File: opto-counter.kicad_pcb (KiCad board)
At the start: 2 copper layers, 27.9 x 27.9 mm, 13 parts, among them J1 IR-REC, J2 qwiic, J3 UPDI, U1 ATtiny404-SS, U2 TSSP6038

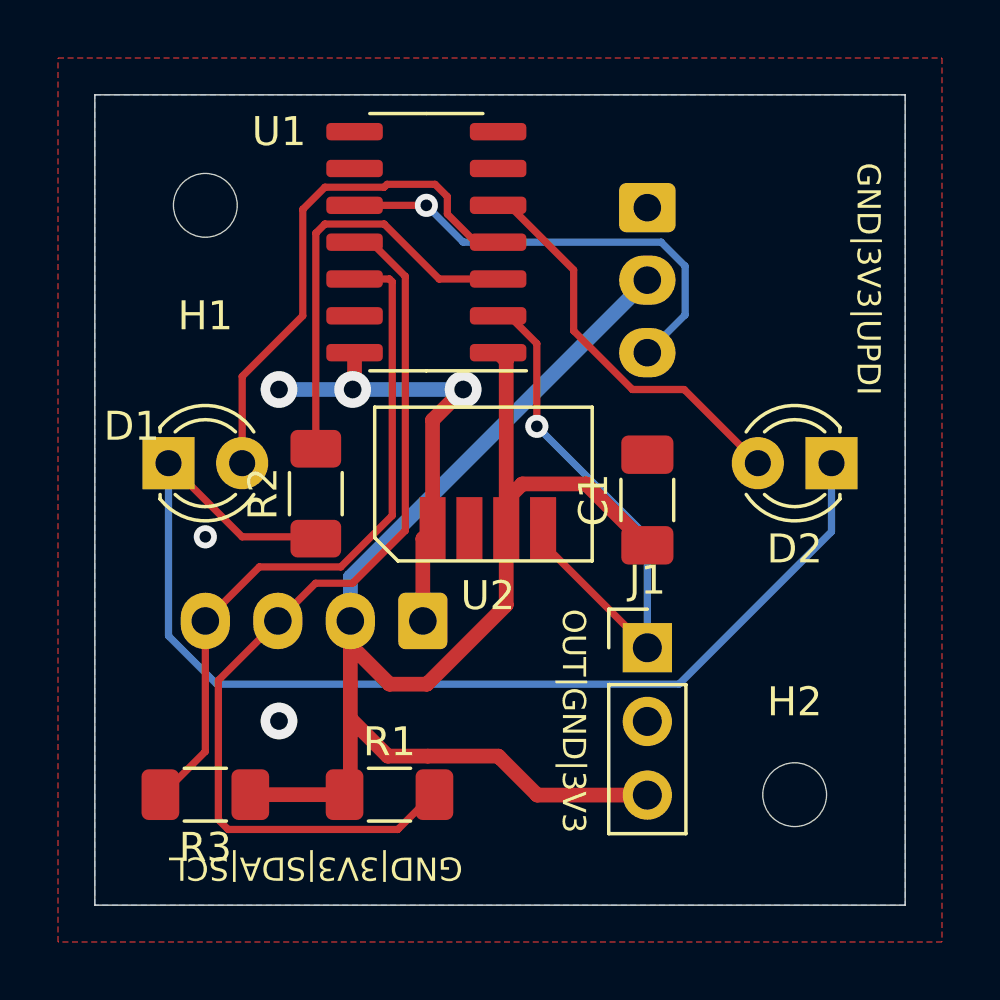
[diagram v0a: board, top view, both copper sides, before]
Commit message: Remove temporary library `opto-counter-rescue`
Also add forgotten `fp-lib-table` and small changes to the PCB.
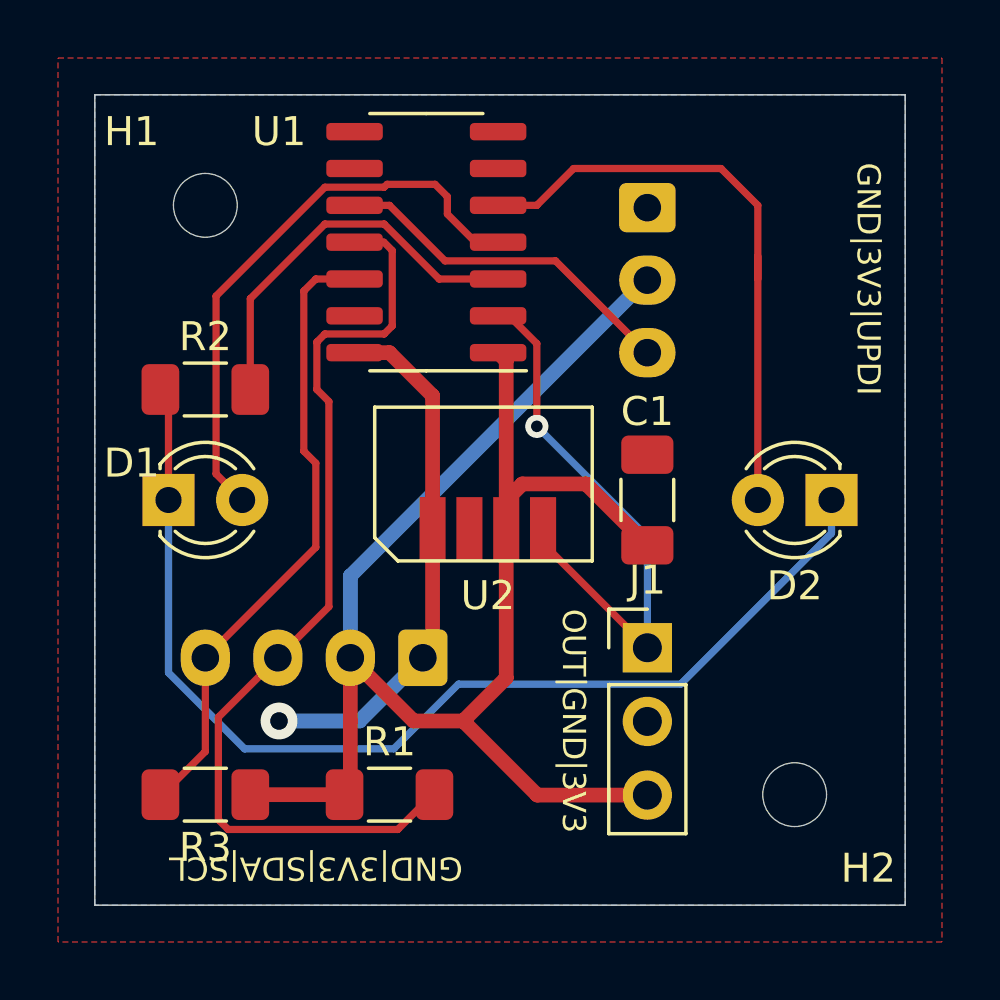
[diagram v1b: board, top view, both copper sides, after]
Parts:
- moved R2 5.24 mm to (67.3, 34.3), turned to 0 degrees
- moved D1 1.27 mm to (66.0, 38.1)
- moved D2 1.27 mm to (88.9, 38.1)
- moved J2 1.27 mm to (74.8, 43.5)
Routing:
- net Net-(D2-A): track 13.9 -> 21.0 mm
- net UPDI: track 15.8 -> 12.2 mm, vias 1 -> 0
- net +3V3: track 59.5 -> 56.4 mm
- net SCL: track 24.0 -> 21.7 mm
- net GND: track 16.2 -> 18.3 mm, vias 5 -> 1
- net Net-(D1-K): track 40.2 -> 38.1 mm
- net Net-(D1-A): track 17.9 -> 19.9 mm
- net Net-(U1-PA5): track 14.7 -> 13.5 mm
- net SDA: track 32.4 -> 33.1 mm

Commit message: Small improvements and fixes in the PCB, generated new gerbers files
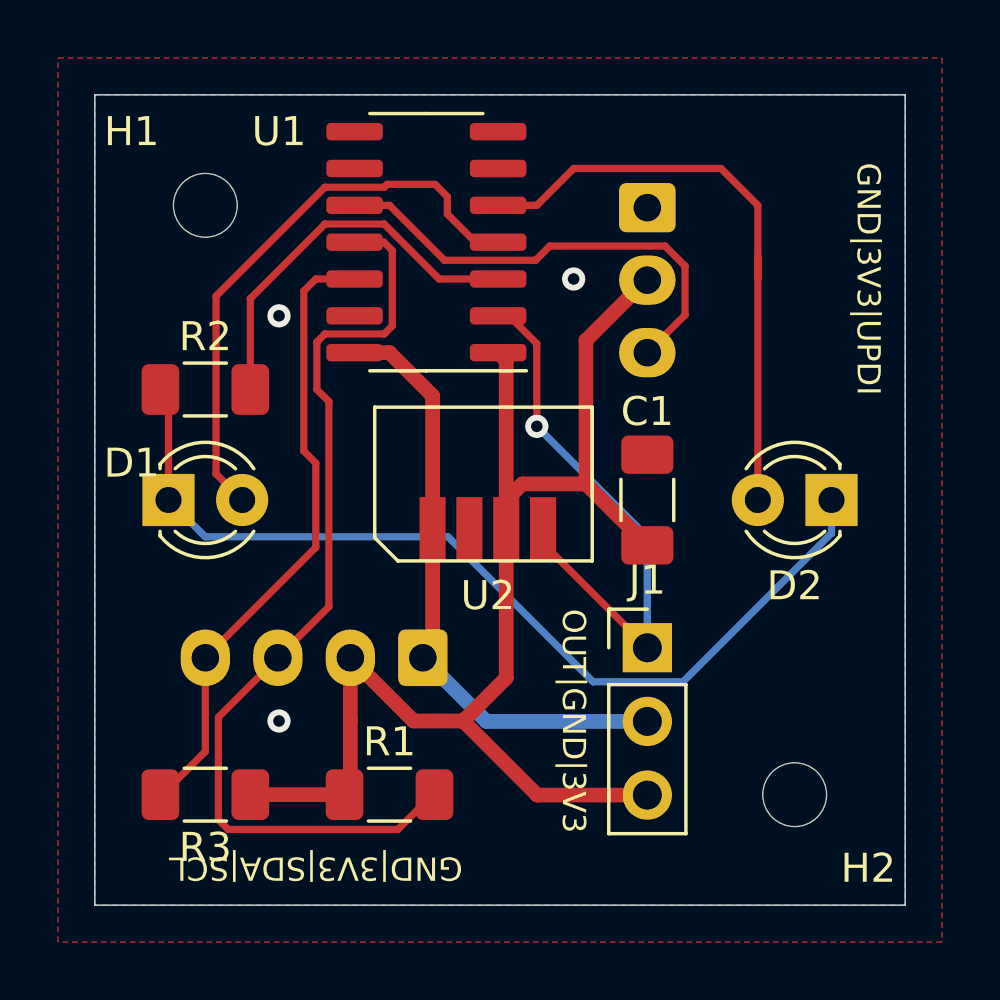
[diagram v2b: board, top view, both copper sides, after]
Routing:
- net +3V3: track 56.4 -> 47.0 mm
- net Net-(D1-K): track 38.1 -> 32.7 mm
- net UPDI: track 12.2 -> 16.2 mm
- net GND: track 18.3 -> 21.1 mm, vias 1 -> 3
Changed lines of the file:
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@@
       (plot_on_all_layers_selection 0x0000000_00000000)
       (disableapertmacros false)
-      (usegerberextensions false)
+      (usegerberextensions true)
       (usegerberattributes true)
       (usegerberadvancedattributes true)
-      (creategerberjobfile true)
+      (creategerberjobfile false)
       (dashed_line_dash_ratio 12.000000)
       (dashed_line_gap_ratio 3.000000)
@@
       (plotinvisibletext false)
       (sketchpadsonfab false)
-      (subtractmaskfromsilk false)
+      (subtractmaskfromsilk true)
       (outputformat 1)
       (mirror false)
@@
     (fp_line (start 1.6 0.8) (end -1.6 0.8)
       (stroke (width 0.1) (type solid)) (layer "F.Fab"))
-    (pad "1" smd roundrect (at -1.5625 0 90) (size 1.325 1.8) (layers "F.Cu" "F.Paste" "F.Mask") (roundrect_rratio 0.188679)
+    (pad "1" smd roundrect (at -1.5625 0 90) (size 1.325 1.8) (layers "F.Cu" "F.Paste" "F.Mask") (roundrect_rratio 0.1886792453)
       (net 1 "+3V3") (pintype "passive"))
-    (pad "2" smd roundrect (at 1.5625 0 90) (size 1.325 1.8) (layers "F.Cu" "F.Paste" "F.Mask") (roundrect_rratio 0.188679)
+    (pad "2" smd roundrect (at 1.5625 0 90) (size 1.325 1.8) (layers "F.Cu" "F.Paste" "F.Mask") (roundrect_rratio 0.1886792453)
       (net 2 "GND") (pintype "passive"))
     (model "${KICAD6_3DMODEL_DIR}/Capacitor_SMD.3dshapes/C_1206_3216Metric.wrl"
@@
     (fp_line (start 1.6 0.8) (end -1.6 0.8)
       (stroke (width 0.1) (type solid)) (layer "F.Fab"))
-    (pad "1" smd roundrect (at -1.55 0) (size 1.3 1.75) (layers "F.Cu" "F.Paste" "F.Mask") (roundrect_rratio 0.192308)
+    (pad "1" smd roundrect (at -1.55 0) (size 1.3 1.75) (layers "F.Cu" "F.Paste" "F.Mask") (roundrect_rratio 0.1923076923)
       (net 1 "+3V3") (pintype "passive"))
-    (pad "2" smd roundrect (at 1.55 0) (size 1.3 1.75) (layers "F.Cu" "F.Paste" "F.Mask") (roundrect_rratio 0.192308)
+    (pad "2" smd roundrect (at 1.55 0) (size 1.3 1.75) (layers "F.Cu" "F.Paste" "F.Mask") (roundrect_rratio 0.1923076923)
       (net 6 "SDA") (pintype "passive"))
     (model "${KICAD6_3DMODEL_DIR}/Resistor_SMD.3dshapes/R_1206_3216Metric.wrl"
@@
     (fp_line (start 1.6 0.8) (end -1.6 0.8)
       (stroke (width 0.1) (type solid)) (layer "F.Fab"))
-    (pad "1" smd roundrect (at -1.55 0) (size 1.3 1.75) (layers "F.Cu" "F.Paste" "F.Mask") (roundrect_rratio 0.192308)
+    (pad "1" smd roundrect (at -1.55 0) (size 1.3 1.75) (layers "F.Cu" "F.Paste" "F.Mask") (roundrect_rratio 0.1923076923)
       (net 3 "Net-(D1-K)") (pintype "passive"))
-    (pad "2" smd roundrect (at 1.55 0) (size 1.3 1.75) (layers "F.Cu" "F.Paste" "F.Mask") (roundrect_rratio 0.192308)
+    (pad "2" smd roundrect (at 1.55 0) (size 1.3 1.75) (layers "F.Cu" "F.Paste" "F.Mask") (roundrect_rratio 0.1923076923)
       (net 9 "Net-(U1-PA5)") (pintype "passive"))
     (model "${KICAD6_3DMODEL_DIR}/Resistor_SMD.3dshapes/R_1206_3216Metric.wrl"
@@
     (fp_line (start 1.6 0.8) (end -1.6 0.8)
       (stroke (width 0.1) (type solid)) (layer "F.Fab"))
-    (pad "1" smd roundrect (at -1.55 0 180) (size 1.3 1.75) (layers "F.Cu" "F.Paste" "F.Mask") (roundrect_rratio 0.192308)
+    (pad "1" smd roundrect (at -1.55 0 180) (size 1.3 1.75) (layers "F.Cu" "F.Paste" "F.Mask") (roundrect_rratio 0.1923076923)
       (net 1 "+3V3") (pintype "passive"))
-    (pad "2" smd roundrect (at 1.55 0 180) (size 1.3 1.75) (layers "F.Cu" "F.Paste" "F.Mask") (roundrect_rratio 0.192308)
+    (pad "2" smd roundrect (at 1.55 0 180) (size 1.3 1.75) (layers "F.Cu" "F.Paste" "F.Mask") (roundrect_rratio 0.1923076923)
       (net 7 "SCL") (pintype "passive"))
     (model "${KICAD6_3DMODEL_DIR}/Resistor_SMD.3dshapes/R_1206_3216Metric.wrl"
@@
     (fp_line (start 9.95 2.3) (end 8.75 2.3)
       (stroke (width 0.1) (type solid)) (layer "B.Fab"))
-    (pad "1" thru_hole roundrect (at 0 0 180) (size 1.7 1.95) (drill 0.95) (layers "*.Cu" "*.Mask") (roundrect_rratio 0.147059)
+    (pad "1" thru_hole roundrect (at 0 0 180) (size 1.7 1.95) (drill 0.95) (layers "*.Cu" "*.Mask") (roundrect_rratio 0.1470588235)
       (net 2 "GND") (pinfunction "Pin_1") (pintype "passive"))
     (pad "2" thru_hole oval (at 2.5 0 180) (size 1.7 1.95) (drill 0.95) (layers "*.Cu" "*.Mask")
@@
     (fp_line (start 7.45 2.3) (end 6.25 2.3)
       (stroke (width 0.1) (type solid)) (layer "B.Fab"))
-    (pad "1" thru_hole roundrect (at 0 0 270) (size 1.7 1.95) (drill 0.95) (layers "*.Cu" "*.Mask") (roundrect_rratio 0.147059)
+    (pad "1" thru_hole roundrect (at 0 0 270) (size 1.7 1.95) (drill 0.95) (layers "*.Cu" "*.Mask") (roundrect_rratio 0.1470588235)
       (net 2 "GND") (pinfunction "Pin_1") (pintype "passive"))
     (pad "2" thru_hole oval (at 2.5 0 270) (size 1.7 1.95) (drill 0.95) (layers "*.Cu" "*.Mask")
@@
   (segment (start 72.31 48.1225) (end 72.31 45.72) (width 0.508) (layer "F.Cu") (net 1))
   (segment (start 72.1725 48.26) (end 72.31 48.1225) (width 0.508) (layer "F.Cu") (net 1))
+  (segment (start 82.55 30.48) (end 80.4335 32.5965) (width 0.508) (layer "F.Cu") (net 1))
   (segment (start 76.2 45.72) (end 74.49 45.72) (width 0.508) (layer "F.Cu") (net 1))
+  (segment (start 82.55 30.52) (end 82.55 30.48) (width 0.508) (layer "F.Cu") (net 1))
   (segment (start 82.55 48.275) (end 78.755 48.275) (width 0.508) (layer "F.Cu") (net 1))
+  (segment (start 80.4335 32.5965) (end 80.4335 37.546) (width 0.508) (layer "F.Cu") (net 1))
   (segment (start 68.7975 48.26) (end 72.1725 48.26) (width 0.508) (layer "F.Cu") (net 1))
   (segment (start 77.685 33.3) (end 77.685 38.1) (width 0.508) (layer "F.Cu") (net 1))
@@
   (segment (start 72.31 45.72) (end 72.31 44.45) (width 0.508) (layer "F.Cu") (net 1))
   (segment (start 77.685 39.1) (end 77.685 44.235) (width 0.508) (layer "F.Cu") (net 1))
-  (segment (start 82.55 30.48) (end 72.31 40.72) (width 0.508) (layer "B.Cu") (net 1))
-  (segment (start 82.55 30.52) (end 82.55 30.48) (width 0.508) (layer "B.Cu") (net 1))
-  (segment (start 72.31 40.72) (end 72.31 43.54) (width 0.508) (layer "B.Cu") (net 1))
   (segment (start 74.81 43.3) (end 75.145 42.965) (width 0.508) (layer "F.Cu") (net 2))
   (segment (start 74.81 43.54) (end 74.81 43.3) (width 0.508) (layer "F.Cu") (net 2))
@@
   (segment (start 75.145 42.965) (end 75.145 39.1) (width 0.508) (layer "F.Cu") (net 2))
   (segment (start 73.66 33.02) (end 72.455 33.02) (width 0.508) (layer "F.Cu") (net 2))
-  (via (at 69.85 45.72) (size 1.27) (drill 0.6096) (layers "F.Cu" "B.Cu") (net 2))
-  (segment (start 74.81 43.54) (end 72.63 45.72) (width 0.508) (layer "B.Cu") (net 2))
-  (segment (start 72.63 45.72) (end 69.85 45.72) (width 0.508) (layer "B.Cu") (net 2))
+  (via (at 69.85 45.72) (size 0.8) (drill 0.4) (layers "F.Cu" "B.Cu") (free) (net 2))
+  (via (at 80.01 30.48) (size 0.8) (drill 0.4) (layers "F.Cu" "B.Cu") (free) (net 2))
+  (via (at 69.85 31.75) (size 0.8) (drill 0.4) (layers "F.Cu" "B.Cu") (free) (net 2))
+  (segment (start 77.005 45.735) (end 74.81 43.54) (width 0.508) (layer "B.Cu") (net 2))
+  (segment (start 82.55 45.735) (end 77.005 45.735) (width 0.508) (layer "B.Cu") (net 2))
   (segment (start 66.04 38.1) (end 66.04 34.57) (width 0.25) (layer "F.Cu") (net 3))
   (segment (start 66.04 34.57) (end 65.76 34.29) (width 0.25) (layer "F.Cu") (net 3))
-  (segment (start 68.663299 46.68) (end 66.04 44.056701) (width 0.25) (layer "B.Cu") (net 3))
-  (segment (start 83.7 44.45) (end 76.038173 44.45) (width 0.25) (layer "B.Cu") (net 3))
-  (segment (start 66.04 44.056701) (end 66.04 38.1) (width 0.25) (layer "B.Cu") (net 3))
-  (segment (start 88.9 39.25) (end 83.7 44.45) (width 0.25) (layer "B.Cu") (net 3))
+  (segment (start 75.681299 39.37) (end 67.31 39.37) (width 0.25) (layer "B.Cu") (net 3))
+  (segment (start 88.9 39.25) (end 83.78 44.37) (width 0.25) (layer "B.Cu") (net 3))
+  (segment (start 67.31 39.37) (end 66.04 38.1) (width 0.25) (layer "B.Cu") (net 3))
+  (segment (start 80.681299 44.37) (end 75.681299 39.37) (width 0.25) (layer "B.Cu") (net 3))
+  (segment (start 83.78 44.37) (end 80.681299 44.37) (width 0.25) (layer "B.Cu") (net 3))
   (segment (start 88.9 38.1) (end 88.9 39.25) (width 0.25) (layer "B.Cu") (net 3))
-  (segment (start 76.038173 44.45) (end 73.808173 46.68) (width 0.25) (layer "B.Cu") (net 3))
-  (segment (start 73.808173 46.68) (end 68.663299 46.68) (width 0.25) (layer "B.Cu") (net 3))
   (segment (start 75.655 27.639695) (end 75.230305 27.215) (width 0.25) (layer "F.Cu") (net 4))
   (segment (start 75.655 28.240305) (end 75.655 27.639695) (width 0.25) (layer "F.Cu") (net 4))
@@
   (segment (start 71.12 39.73) (end 71.12 36.83) (width 0.25) (layer "F.Cu") (net 7))
   (segment (start 70.705 36.415) (end 70.705 30.895) (width 0.25) (layer "F.Cu") (net 7))
+  (segment (start 83.85 30.033299) (end 83.161701 29.345) (width 0.25) (layer "F.Cu") (net 8))
+  (segment (start 75.555 29.835) (end 73.66 27.94) (width 0.25) (layer "F.Cu") (net 8))
   (segment (start 73.66 27.94) (end 72.455 27.94) (width 0.25) (layer "F.Cu") (net 8))
-  (segment (start 82.55 33.02) (end 79.385 29.855) (width 0.25) (layer "F.Cu") (net 8))
-  (segment (start 75.575 29.855) (end 73.66 27.94) (width 0.25) (layer "F.Cu") (net 8))
-  (segment (start 79.385 29.855) (end 75.575 29.855) (width 0.25) (layer "F.Cu") (net 8))
+  (segment (start 79.186751 29.345) (end 78.696751 29.835) (width 0.25) (layer "F.Cu") (net 8))
+  (segment (start 83.161701 29.345) (end 79.186751 29.345) (width 0.25) (layer "F.Cu") (net 8))
+  (segment (start 78.696751 29.835) (end 75.555 29.835) (width 0.25) (layer "F.Cu") (net 8))
+  (segment (start 83.85 31.72) (end 83.85 30.033299) (width 0.25) (layer "F.Cu") (net 8))
+  (segment (start 82.55 33.02) (end 83.85 31.72) (width 0.25) (layer "F.Cu") (net 8))
   (segment (start 73.476751 28.585) (end 71.433249 28.585) (width 0.25) (layer "F.Cu") (net 9))
   (segment (start 68.86 34.29) (end 68.86 31.158249) (width 0.25) (layer "F.Cu") (net 9))

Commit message: Use ATtiny1614-SS as the mCPU
Actually, we're targetting to ATtiny3224, which should be pin
compatible.
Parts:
- U1: value ATtiny404-SS -> ATtiny1614-SS
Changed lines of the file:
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@@
     (descr "SOIC, 14 Pin (JEDEC MS-012AB, https://www.analog.com/media/en/package-pcb-resources/package/pkg_pdf/soic_narrow-r/r_14.pdf), generated with kicad-footprint-generator ipc_gullwing_generator.py")
     (tags "SOIC SO")
-    (property "Mfg" "ATTINY404-SSFR")
     (property "Sheetfile" "opto-counter.kicad_sch")
     (property "Sheetname" "")
-    (property "ki_description" "20MHz, 4kB Flash, 256B SRAM, 128B EEPROM, SOIC-14")
+    (property "ki_description" "20MHz, 16kB Flash, 2kB SRAM, 256B EEPROM, SOIC-14")
     (property "ki_keywords" "AVR 8bit Microcontroller tinyAVR")
     (attr smd)
@@
         (effects (font (size 1 1) (thickness 0.15)))
     )
-    (fp_text value "ATtiny404-SS" (at 0 5.28) (layer "F.Fab")
+    (fp_text value "ATtiny1614-SS" (at 0 5.28) (layer "F.Fab")
         (effects (font (size 1 1) (thickness 0.15)))
     )
